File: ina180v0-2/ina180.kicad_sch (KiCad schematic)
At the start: 6 parts, among them U1 INA180A2

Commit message: Improved schematic
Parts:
- CF1: renamed from Cf1; value 8n -> 8nF
- RSENSE: renamed from RSHUNT1; value R010 -> R005
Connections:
- net GND: no longer RF2.2, RSENSE.2
- net VIN+ renamed IN+
- net VS renamed VCC
- new net IN-: RF2.2, RSENSE.2
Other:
- note added: "CURRENT SENSE AMPLIFIER"
- note added: "Includes input low pass filter to reduce input noise"
- note added: "Output goes to a voltage divider and a voltage follower circuit"
- note added: "TEXAS INSTRUMENTS INA180A2 G=100V/1V"
- moved on the sheet: C1, RF1, RF2

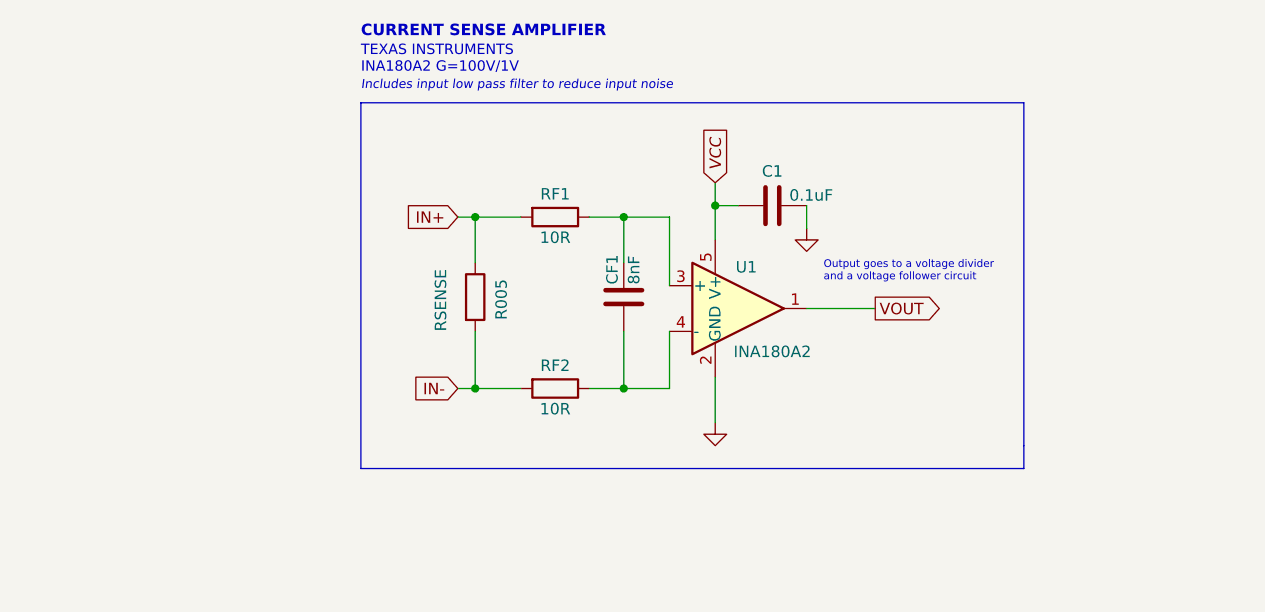
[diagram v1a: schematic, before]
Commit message: Added power flags and changed to nets
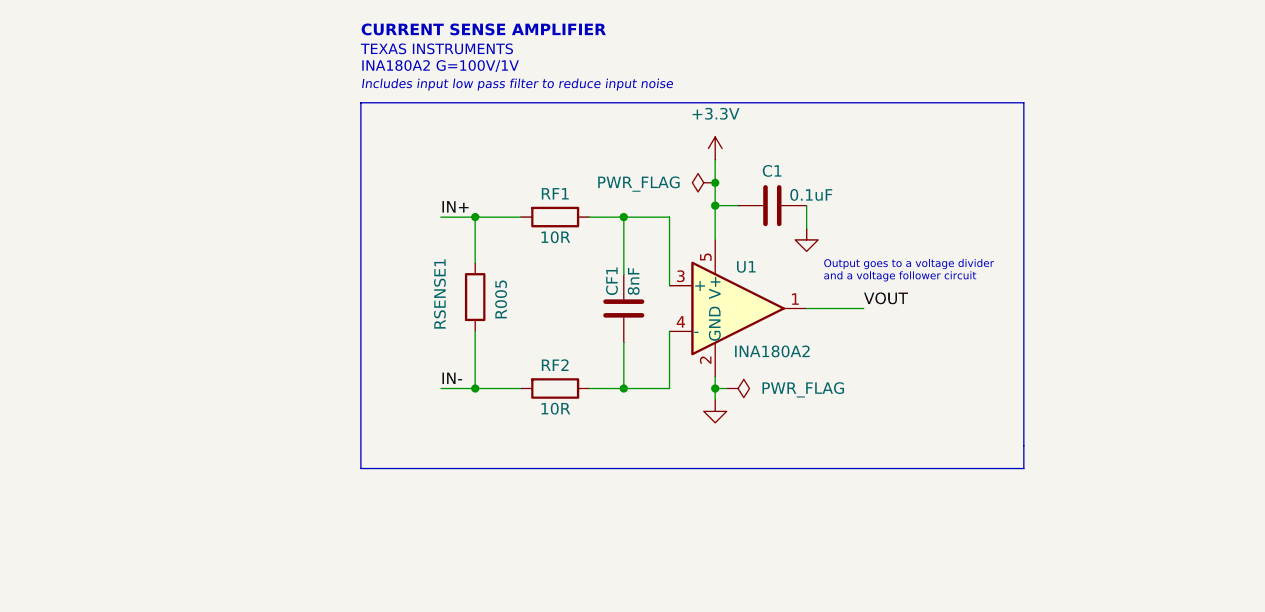
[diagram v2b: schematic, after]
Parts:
- renumbered RSENSE to RSENSE1
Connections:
- net VCC renamed +3.3V
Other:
- moved on the sheet: CF1

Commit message: Removed comment and adjusted schematic borders
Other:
- note removed: "Output goes to a voltage divider and a voltage follower circuit"
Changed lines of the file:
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@@
   (junction (at 129.54 71.12) (diameter 0) (color 0 0 0 0)
   )
-  (polyline (pts (xy 90.17 102.87) (xy 163.83 102.87))
-    (stroke (width 0) (type default) (color 0 0 0 0))
-  )
   (wire (pts (xy 129.54 71.12) (xy 129.54 73.66))
     (stroke (width 0) (type default) (color 0 0 0 0))
   )
-  (polyline (pts (xy 163.83 100.33) (xy 163.83 62.23))
-    (stroke (width 0) (type default) (color 0 0 0 0))
-  )
   (wire (pts (xy 119.38 74.93) (xy 124.46 74.93))
     (stroke (width 0) (type default) (color 0 0 0 0))
@@
     (stroke (width 0) (type default) (color 0 0 0 0))
   )
+  (polyline (pts (xy 153.67 99.06) (xy 153.67 62.23))
+    (stroke (width 0) (type default) (color 0 0 0 0))
+  )
   (wire (pts (xy 99.06 93.98) (xy 102.87 93.98))
     (stroke (width 0) (type default) (color 0 0 0 0))
@@
     (stroke (width 0) (type default) (color 0 0 0 0))
   )
+  (polyline (pts (xy 90.17 99.06) (xy 153.67 99.06))
+    (stroke (width 0) (type default) (color 0 0 0 0))
+  )
   (wire (pts (xy 115.57 93.98) (xy 119.38 93.98))
     (stroke (width 0) (type default) (color 0 0 0 0))
   )
-  (polyline (pts (xy 163.83 102.87) (xy 163.83 100.33))
-    (stroke (width 0) (type default) (color 0 0 0 0))
-  )
   (wire (pts (xy 119.38 88.9) (xy 119.38 93.98))
     (stroke (width 0) (type default) (color 0 0 0 0))
@@
     (stroke (width 0) (type default) (color 0 0 0 0))
   )
-  (polyline (pts (xy 163.83 62.23) (xy 90.17 62.23))
+  (polyline (pts (xy 153.67 62.23) (xy 90.17 62.23))
     (stroke (width 0) (type default) (color 0 0 0 0))
   )
@@
     (stroke (width 0) (type default) (color 0 0 0 0))
   )
-  (polyline (pts (xy 90.17 62.23) (xy 90.17 102.87))
+  (polyline (pts (xy 90.17 62.23) (xy 90.17 99.06))
     (stroke (width 0) (type default) (color 0 0 0 0))
   )
@@
     (effects (font (size 1 1) italic) (justify left bottom))
   )
-  (text "Output goes to a voltage divider\nand a voltage follower circuit"
-    (at 141.5796 82.1944 0)
-    (effects (font (size 0.85 0.85)) (justify left bottom))
-  )
   (label "VOUT" (at 146.05 85.09 0)
     (effects (font (size 1.27 1.27)) (justify left bottom))
@@
   )
   (symbol (lib_id "power:+3.3V") (at 129.54 68.58 0) (unit 1)
-    (in_bom yes) (on_board yes) (fields_autoplaced)
+    (in_bom yes) (on_board yes)
     (property "Reference" "#3V03" (id 0) (at 129.54 72.39 0)
       (effects (font (size 1.27 1.27)) hide)
     )
-    (property "Value" "+3.3V" (id 1) (at 129.54 63.5 0))
+    (property "Value" "+3.3V" (id 1) (at 129.54 64.77 0))
     (property "Footprint" "" (id 2) (at 129.54 68.58 0)
       (effects (font (size 1.27 1.27)) hide)

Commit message: Adjusted capacitor values
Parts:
- C1: value 0.1uF -> 100n
- CF1: value 8nF -> 8n
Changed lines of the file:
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@@
     (in_bom yes) (on_board yes)
     (property "Reference" "C1" (id 0) (at 135.89 69.85 90))
-    (property "Value" "0.1uF" (id 1) (at 140.208 72.517 90))
+    (property "Value" "100n" (id 1) (at 140.208 72.517 90))
     (property "Footprint" "Capacitor_SMD:C_0603_1608Metric" (id 2) (at 139.7 72.6948 0)
       (effects (font (size 1.27 1.27)) hide)
@@
   (symbol (lib_id "Device:C") (at 119.38 85.09 0) (unit 1)
     (in_bom yes) (on_board yes)
-    (property "Reference" "CF1" (id 0) (at 118.11 83.693 90)
+    (property "Reference" "CF1" (id 0) (at 113.03 85.09 0)
       (effects (font (size 1.27 1.27)) (justify left))
     )
-    (property "Value" "8nF" (id 1) (at 120.523 83.693 90)
+    (property "Value" "8n" (id 1) (at 119.38 82.55 0)
       (effects (font (size 1.27 1.27)) (justify left))
     )
@@
     )
     (path "/1e94f8fc-0c4e-47e8-8f9d-fa87f7582139"
-      (reference "C1") (unit 1) (value "0.1uF") (footprint "Capacitor_SMD:C_0603_1608Metric")
+      (reference "C1") (unit 1) (value "100n") (footprint "Capacitor_SMD:C_0603_1608Metric")
     )
     (path "/73ae3780-85f7-4747-9283-ab51e69a57ba"
-      (reference "CF1") (unit 1) (value "8nF") (footprint "Capacitor_SMD:C_0603_1608Metric")
+      (reference "CF1") (unit 1) (value "8n") (footprint "Capacitor_SMD:C_0603_1608Metric")
     )
     (path "/c31d1262-cebc-4060-83ae-b4004e0ebdbb"

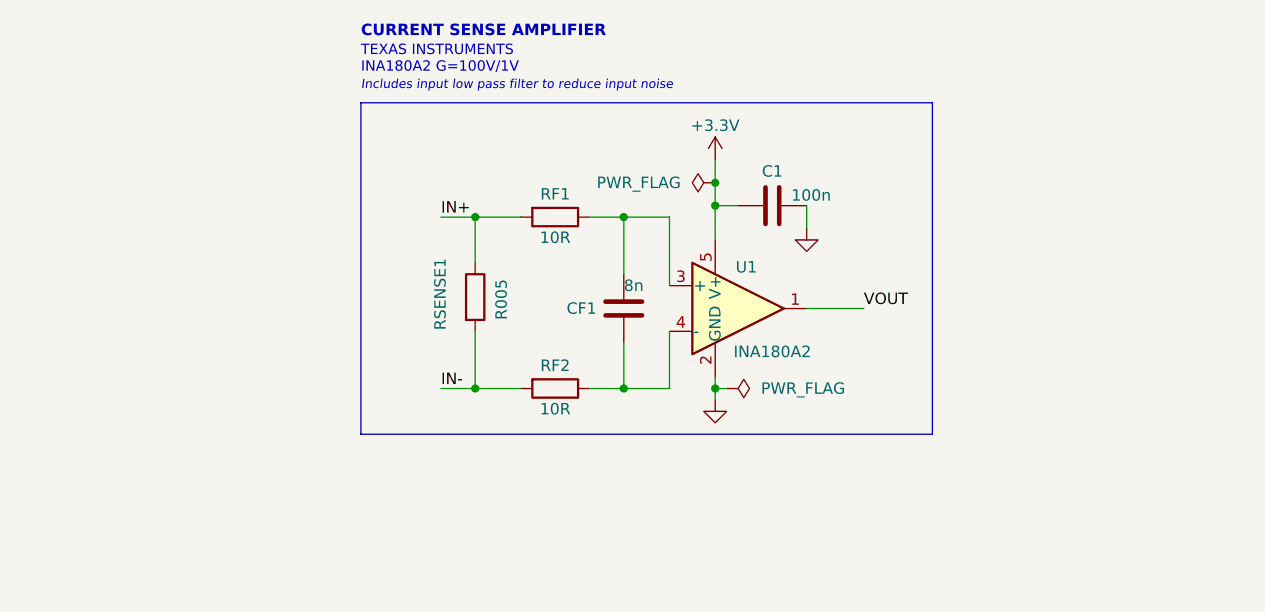
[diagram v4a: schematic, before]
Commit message: Added footprints for terminal, and updated schematic
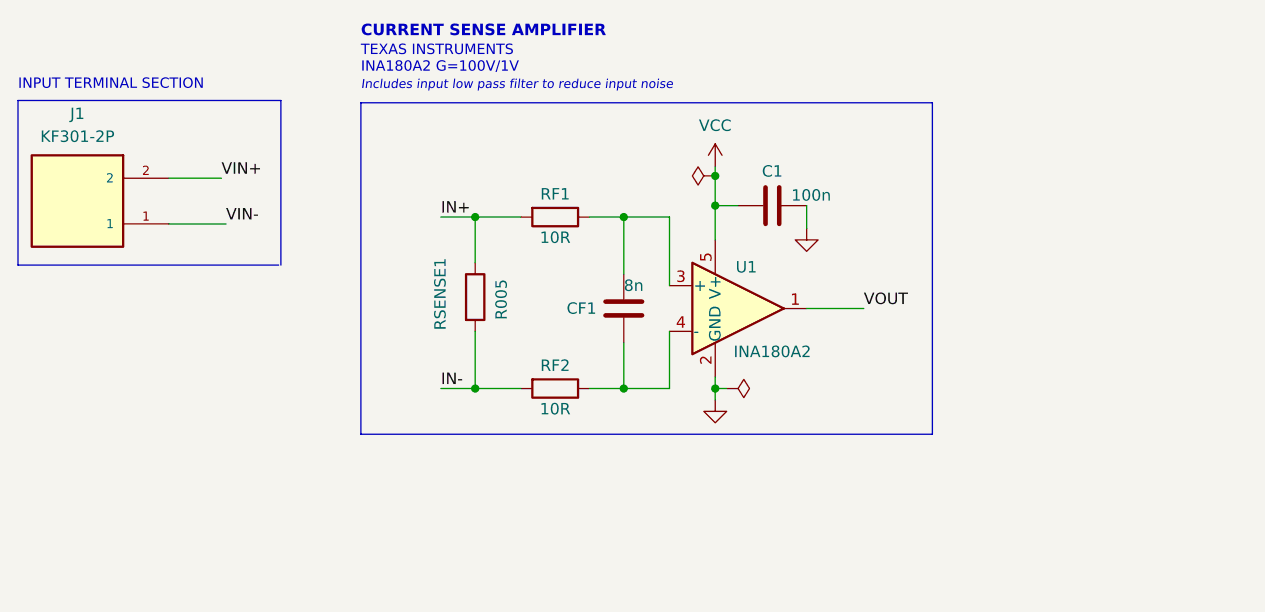
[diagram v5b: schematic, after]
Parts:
- added J1: KF301-2P, KF301:HANDSON_KF301-2P, symbol KF301-2P:KF301-2P
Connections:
- net +3.3V renamed VCC
- new net VIN+: J1.2
- new net VIN-: J1.1
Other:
- note added: "INPUT TERMINAL SECTION"
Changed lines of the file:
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@@
   (junction (at 119.38 93.98) (diameter 0) (color 0 0 0 0)
   )
-  (junction (at 129.54 71.12) (diameter 0) (color 0 0 0 0)
-  )
-  (wire (pts (xy 129.54 71.12) (xy 129.54 73.66))
+  (junction (at 129.54 70.358) (diameter 0) (color 0 0 0 0)
+  )
+  (polyline (pts (xy 81.026 80.264) (xy 52.07 80.264))
+    (stroke (width 0) (type default) (color 0 0 0 0))
+  )
+  (wire (pts (xy 129.54 73.66) (xy 132.08 73.66))
+    (stroke (width 0) (type default) (color 0 0 0 0))
+  )
+  (polyline (pts (xy 52.07 80.264) (xy 52.07 61.976))
+    (stroke (width 0) (type default) (color 0 0 0 0))
+  )
+  (wire (pts (xy 129.54 73.66) (xy 129.54 77.47))
     (stroke (width 0) (type default) (color 0 0 0 0))
   )
@@
     (stroke (width 0) (type default) (color 0 0 0 0))
   )
-  (wire (pts (xy 129.54 68.58) (xy 129.54 71.12))
+  (polyline (pts (xy 52.07 61.976) (xy 81.28 61.976))
+    (stroke (width 0) (type default) (color 0 0 0 0))
+  )
+  (polyline (pts (xy 81.28 61.976) (xy 81.28 80.264))
     (stroke (width 0) (type default) (color 0 0 0 0))
   )
@@
     (stroke (width 0) (type default) (color 0 0 0 0))
   )
-  (wire (pts (xy 129.54 73.66) (xy 129.54 77.47))
-    (stroke (width 0) (type default) (color 0 0 0 0))
-  )
-  (wire (pts (xy 129.54 73.66) (xy 132.08 73.66))
+  (wire (pts (xy 68.834 70.612) (xy 74.676 70.612))
     (stroke (width 0) (type default) (color 0 0 0 0))
   )
@@
     (stroke (width 0) (type default) (color 0 0 0 0))
   )
+  (wire (pts (xy 129.54 69.342) (xy 129.54 70.358))
+    (stroke (width 0) (type default) (color 0 0 0 0))
+  )
   (wire (pts (xy 102.87 74.93) (xy 102.87 80.01))
     (stroke (width 0) (type default) (color 0 0 0 0))
@@
     (stroke (width 0) (type default) (color 0 0 0 0))
   )
+  (wire (pts (xy 129.54 70.358) (xy 129.54 73.66))
+    (stroke (width 0) (type default) (color 0 0 0 0))
+  )
   (wire (pts (xy 102.87 74.93) (xy 107.95 74.93))
     (stroke (width 0) (type default) (color 0 0 0 0))
   )
   (polyline (pts (xy 90.17 62.23) (xy 90.17 99.06))
+    (stroke (width 0) (type default) (color 0 0 0 0))
+  )
+  (wire (pts (xy 68.834 75.692) (xy 75.184 75.692))
     (stroke (width 0) (type default) (color 0 0 0 0))
   )
@@
     (effects (font (size 1 1) italic) (justify left bottom))
   )
+  (text "INPUT TERMINAL SECTION\n" (at 52.07 60.96 0)
+    (effects (font (size 1.15 1.15)) (justify left bottom))
+  )
   (label "VOUT" (at 146.05 85.09 0)
     (effects (font (size 1.27 1.27)) (justify left bottom))
   )
+  (label "VIN+" (at 74.676 70.612 0)
+    (effects (font (size 1.27 1.27)) (justify left bottom))
+  )
   (label "IN-" (at 99.06 93.98 0)
     (effects (font (size 1.27 1.27)) (justify left bottom))
   )
+  (label "VIN-" (at 75.184 75.692 0)
+    (effects (font (size 1.27 1.27)) (justify left bottom))
+  )
   (label "IN+" (at 99.06 74.93 0)
     (effects (font (size 1.27 1.27)) (justify left bottom))
-  )
-  (symbol (lib_id "power:PWR_FLAG") (at 129.54 71.12 90) (unit 1)
-    (in_bom yes) (on_board yes) (fields_autoplaced)
-    (property "Reference" "#FLG01" (id 0) (at 127.635 71.12 0)
-      (effects (font (size 1.27 1.27)) hide)
-    )
-    (property "Value" "PWR_FLAG" (id 1) (at 125.73 71.1199 90)
-      (effects (font (size 1.27 1.27)) (justify left))
-    )
-    (property "Footprint" "" (id 2) (at 129.54 71.12 0)
-      (effects (font (size 1.27 1.27)) hide)
-    )
-    (property "Datasheet" "~" (id 3) (at 129.54 71.12 0)
-      (effects (font (size 1.27 1.27)) hide)
-    )
-    (pin "1")
   )
   (symbol (lib_id "Device:C") (at 135.89 73.66 90) (unit 1)
@@
     (pin "2")
   )
+  (symbol (lib_id "power:PWR_FLAG") (at 129.54 70.358 90) (unit 1)
+    (in_bom yes) (on_board yes) (fields_autoplaced)
+    (property "Reference" "#VCC02" (id 0) (at 127.635 70.358 0)
+      (effects (font (size 1.27 1.27)) hide)
+    )
+    (property "Value" "PWR_FLAG" (id 1) (at 125.73 70.3579 90)
+      (effects (font (size 1.27 1.27)) (justify left) hide)
+    )
+    (property "Footprint" "" (id 2) (at 129.54 70.358 0)
+      (effects (font (size 1.27 1.27)) hide)
+    )
+    (property "Datasheet" "~" (id 3) (at 129.54 70.358 0)
+      (effects (font (size 1.27 1.27)) hide)
+    )
+    (pin "1")
+  )
   (symbol (lib_id "Device:R") (at 111.76 93.98 270) (unit 1)
     (in_bom yes) (on_board yes)
@@
   (symbol (lib_id "power:GND") (at 129.54 95.25 0) (unit 1)
     (in_bom yes) (on_board yes) (fields_autoplaced)
-    (property "Reference" "#GND0101" (id 0) (at 129.54 101.6 0)
+    (property "Reference" "#GND01" (id 0) (at 129.54 101.6 0)
       (effects (font (size 1.27 1.27)) hide)
     )
@@
     )
     (pin "1")
+  )
+  (symbol (lib_id "KF301-2P:KF301-2P") (at 58.674 73.152 180) (unit 1)
+    (in_bom yes) (on_board yes) (fields_autoplaced)
+    (property "Reference" "J1" (id 0) (at 58.674 63.4492 0))
+    (property "Value" "KF301-2P" (id 1) (at 58.674 65.9892 0))
+    (property "Footprint" "KF301:HANDSON_KF301-2P" (id 2) (at 58.674 73.152 0)
+      (effects (font (size 1.27 1.27)) (justify bottom) hide)
+    )
+    (property "Datasheet" "" (id 3) (at 58.674 73.152 0)
+      (effects (font (size 1.27 1.27)) hide)
+    )
+    (property "STANDARD" "Manufacturer Recommendations" (id 4) (at 58.674 73.152 0)
+      (effects (font (size 1.27 1.27)) (justify bottom) hide)
+    )
+    (property "PARTREV" "NA" (id 5) (at 58.674 73.152 0)
+      (effects (font (size 1.27 1.27)) (justify bottom) hide)
+    )
+    (property "MANUFACTURER" "Handson Technology" (id 6) (at 58.674 73.152 0)
+      (effects (font (size 1.27 1.27)) (justify bottom) hide)
+    )
+    (property "MAXIMUM_PACKAGE_HEIGHT" "10mm" (id 7) (at 58.674 73.152 0)
+      (effects (font (size 1.27 1.27)) (justify bottom) hide)
+    )
+    (pin "1")
+    (pin "2")
   )
   (symbol (lib_id "Device:C") (at 119.38 85.09 0) (unit 1)
@@
   (symbol (lib_id "power:PWR_FLAG") (at 130.81 93.98 270) (unit 1)
     (in_bom yes) (on_board yes) (fields_autoplaced)
-    (property "Reference" "#FLG02" (id 0) (at 132.715 93.98 0)
+    (property "Reference" "#GND03" (id 0) (at 132.715 93.98 0)
       (effects (font (size 1.27 1.27)) hide)
     )
     (property "Value" "PWR_FLAG" (id 1) (at 134.62 93.9799 90)
-      (effects (font (size 1.27 1.27)) (justify left))
+      (effects (font (size 1.27 1.27)) (justify left) hide)
     )
     (property "Footprint" "" (id 2) (at 130.81 93.98 0)
@@
     (pin "2")
   )
+  (symbol (lib_id "power:VCC") (at 129.54 69.342 0) (unit 1)
+    (in_bom yes) (on_board yes) (fields_autoplaced)
+    (property "Reference" "#VCC01" (id 0) (at 129.54 73.152 0)
+      (effects (font (size 1.27 1.27)) hide)
+    )
+    (property "Value" "VCC" (id 1) (at 129.54 64.77 0))
+    (property "Footprint" "" (id 2) (at 129.54 69.342 0)
+      (effects (font (size 1.27 1.27)) hide)
+    )
+    (property "Datasheet" "" (id 3) (at 129.54 69.342 0)
+      (effects (font (size 1.27 1.27)) hide)
+    )
+    (pin "1")
+  )
   (symbol (lib_id "power:GND") (at 139.7 76.2 0) (unit 1)
     (in_bom yes) (on_board yes)
@@
     (pin "1")
   )
-  (symbol (lib_id "power:+3.3V") (at 129.54 68.58 0) (unit 1)
-    (in_bom yes) (on_board yes)
-    (property "Reference" "#3V03" (id 0) (at 129.54 72.39 0)
-      (effects (font (size 1.27 1.27)) hide)
-    )
-    (property "Value" "+3.3V" (id 1) (at 129.54 64.77 0))
-    (property "Footprint" "" (id 2) (at 129.54 68.58 0)
-      (effects (font (size 1.27 1.27)) hide)
-    )
-    (property "Datasheet" "" (id 3) (at 129.54 68.58 0)
-      (effects (font (size 1.27 1.27)) hide)
-    )
-    (pin "1")
-  )
   (sheet_instances
     (path "/" (page "1"))
   )
   (symbol_instances
-    (path "/f1416d7b-b720-4859-ad35-7c041781288d"
-      (reference "#3V03") (unit 1) (value "+3.3V") (footprint "")
-    )
-    (path "/1e515220-13c8-45d7-af85-a58dc35acfd6"
-      (reference "#FLG01") (unit 1) (value "PWR_FLAG") (footprint "")
-    )
-    (path "/98b55fa6-95c2-43e9-ac64-bb7219434b41"
-      (reference "#FLG02") (unit 1) (value "PWR_FLAG") (footprint "")
+    (path "/4e741221-b46b-4cd2-8602-61310a39c811"
+      (reference "#GND01") (unit 1) (value "GND") (footprint "")
     )
     (path "/ef72b2a5-461e-445b-a71e-29f3da9332fc"
       (reference "#GND02") (unit 1) (value "GND") (footprint "")
     )
-    (path "/4e741221-b46b-4cd2-8602-61310a39c811"
-      (reference "#GND0101") (unit 1) (value "GND") (footprint "")
+    (path "/98b55fa6-95c2-43e9-ac64-bb7219434b41"
+      (reference "#GND03") (unit 1) (value "PWR_FLAG") (footprint "")
+    )
+    (path "/cc0627c9-ae88-4ca7-abfc-fb10b3d5a687"
+      (reference "#VCC01") (unit 1) (value "VCC") (footprint "")
+    )
+    (path "/3430f91c-86a6-4b87-8967-7173359c3946"
+      (reference "#VCC02") (unit 1) (value "PWR_FLAG") (footprint "")
     )
     (path "/1e94f8fc-0c4e-47e8-8f9d-fa87f7582139"
@@
       (reference "CF1") (unit 1) (value "8n") (footprint "Capacitor_SMD:C_0603_1608Metric")
     )
+    (path "/52e7a8b9-3aa5-4845-819d-cb737016585e"
+      (reference "J1") (unit 1) (value "KF301-2P") (footprint "KF301:HANDSON_KF301-2P")
+    )
     (path "/c31d1262-cebc-4060-83ae-b4004e0ebdbb"

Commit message: Fixed schematic and added first pcb preview
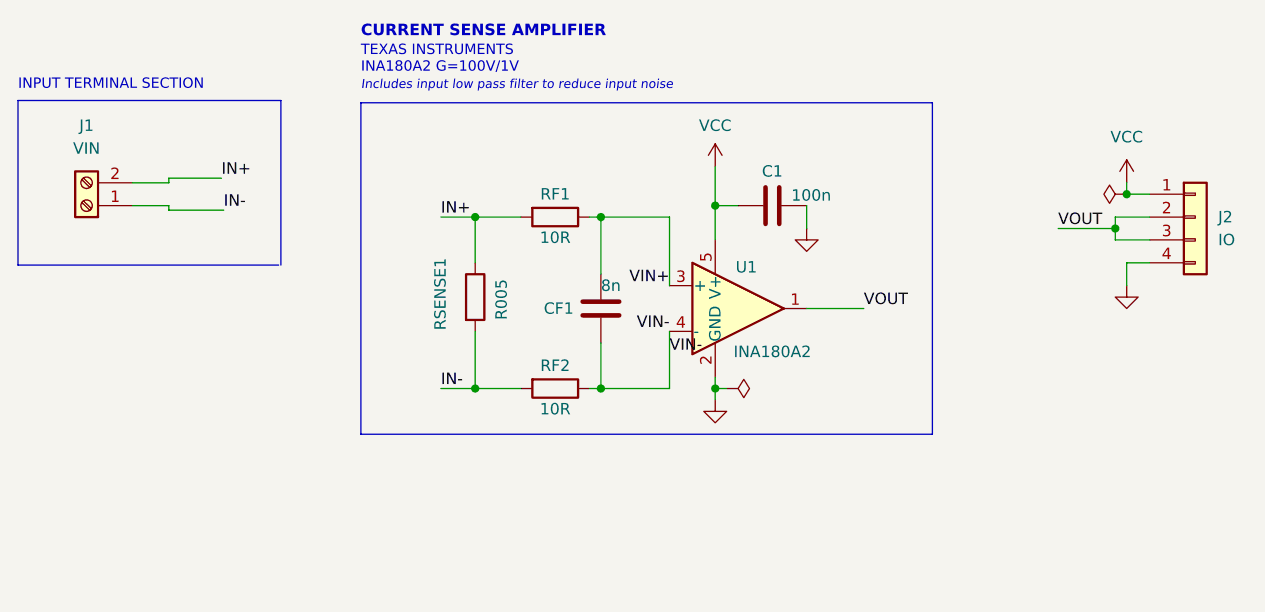
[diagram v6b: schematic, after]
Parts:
- removed J1: KF301-2P, KF301:HANDSON_KF301-2P, symbol KF301-2P:KF301-2P
- added J1: VIN, symbol Connector:Screw_Terminal_01x02
- added J2: IO, symbol Connector_Generic:Conn_01x04
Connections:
- net GND: now also J2.4 (Pin_4)
- net IN+: now also J1.2 (Pin_2)
- net IN-: now also J1.1 (Pin_1)
- net VCC: now also J2.1 (Pin_1)
- net VIN+: now also CF1.1, RF1.1, U1.3 (+)
- net VIN-: now also CF1.2, RF2.1, U1.4 (-)
- net VOUT: now also J2.2 (Pin_2), J2.3 (Pin_3)
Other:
- moved on the sheet: CF1
